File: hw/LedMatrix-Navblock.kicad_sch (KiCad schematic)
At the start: 38 parts, among them Q4200 DTA114E, Q4201 DTA114E, Q4202 DTA114E, Q4203 DTA114E, Q4204 DTA114E, Q4205 DTC114EE, Q4206 DTC114EE, Q4207 DTC114EE, Q4208 DTC114EE, Q4209 DTC114EE, Q4210 DTC114EE, Q4211 DTC114EE, Q4212 DTC114EE, Q4213 DTC114EE

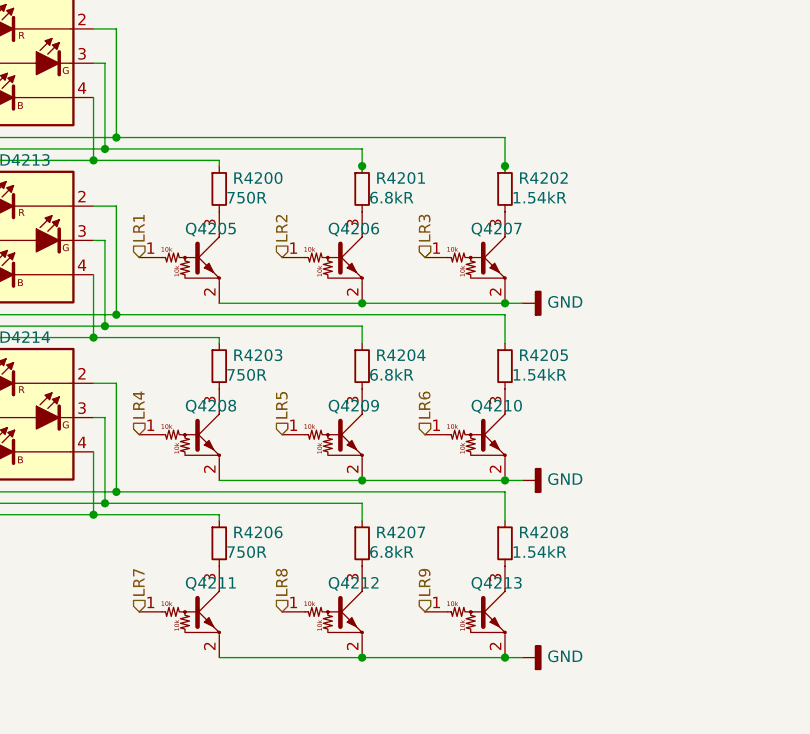
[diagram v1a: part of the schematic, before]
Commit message: Adjust LED matrix resistors.
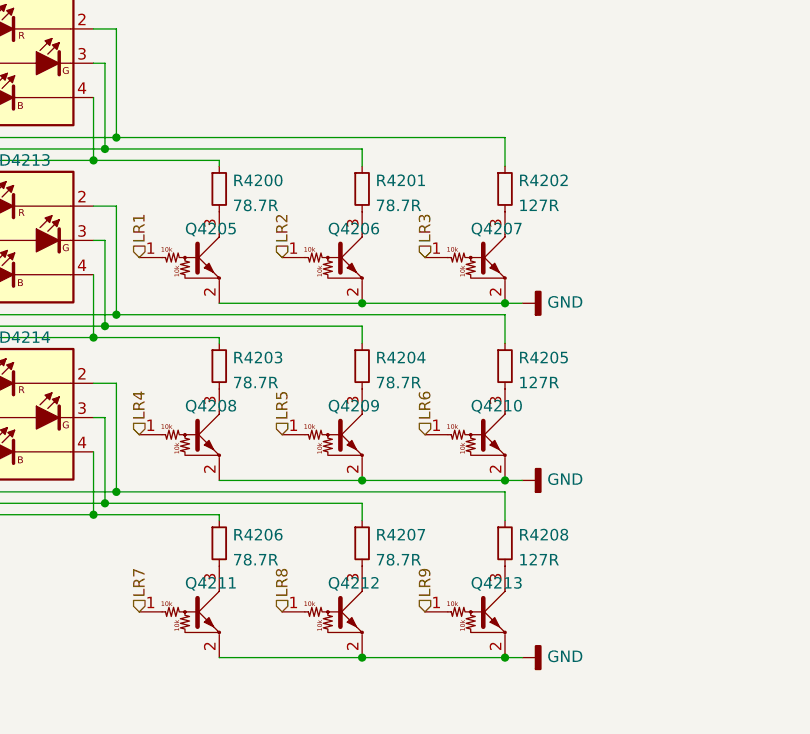
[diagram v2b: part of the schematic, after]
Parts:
- removed R4200, R4203, R4206: 750R, Keyboard:R_0402, symbol Keyboard:750R
- removed R4201, R4204, R4207: 6.8kR, Keyboard:R_0402, symbol Keyboard:6.8kR
- removed R4202, R4205, R4208: 1.54kR, Keyboard:R_0402, symbol Keyboard:1.54kR
- added R4200, R4201, R4203, R4204, R4206, R4207: 78.7R, Keyboard:R_0402, symbol Keyboard:78.7R
- added R4202, R4205, R4208: 127R, Keyboard:R_0402, symbol Keyboard:127R
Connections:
- net at D4200.2 (KR), D4203.2 (KR), D4206.2 (KR)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: now also R4202.1
- net at D4200.3 (KG), D4203.3 (KG), D4206.3 (KG)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: now also R4201.1
- net at D4200.4 (KB), D4203.4 (KB), D4206.4 (KB)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: now also R4200.1
- net at D4201.2 (KR), D4204.2 (KR), D4207.2 (KR)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: now also R4205.1
- net at D4201.3 (KG), D4204.3 (KG), D4207.3 (KG)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: now also R4204.1
- net at D4201.4 (KB), D4204.4 (KB), D4207.4 (KB)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: now also R4203.1
- net at D4202.2 (KR), D4205.2 (KR), D4208.2 (KR)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: now also R4208.1
- net at D4202.3 (KG), D4205.3 (KG), D4208.3 (KG)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: now also R4207.1
- net at D4202.4 (KB), D4205.4 (KB), D4208.4 (KB)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: now also R4206.1
- net at Q4205.3 (C): now also R4200.2
- net at Q4213.3 (C): now also R4208.2
- net at Q4212.3 (C): now also R4207.2
- net at Q4211.3 (C): now also R4206.2
- net at Q4210.3 (C): now also R4205.2
- net at Q4209.3 (C): now also R4204.2
- net at Q4208.3 (C): now also R4203.2
- net at Q4207.3 (C): now also R4202.2
- net at Q4206.3 (C): now also R4201.2
